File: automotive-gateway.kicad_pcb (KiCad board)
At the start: 2 copper layers, 101.6 x 88.9 mm, 103 parts, among them J3 Conn_01x02_Pin, Q1 AO3401A, Q2 2N7002, U1 STM32F405RGTx, U10 TJA1021xT, U11 TJA1021xT, U2 STM32F405RGTx, U3 ESP32-WROOM-32UE, U4 TJA1044GT-3, U5 TJA1044GT-3, U6 TJA1055T/3, U7 TJA1055T/3, U8 LM2596S-5, U9 AMS1117-3.3

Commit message: updated logo
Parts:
- moved G*** 1.26 mm to (107.8, 84.3)
- moved G*** 0.82 mm to (70.3, 20.4)
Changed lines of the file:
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@@
 	(footprint "Logos:logo_lhe"
 		(layer "F.Cu")
-		(at 108.0008 83.058 90)
+		(at 107.846144 84.310827 90)
 		(property "Reference" "G***"
 			(at 0 0 90)
@@
 	(footprint "mylib:logo_ag_12mm"
 		(layer "F.Cu")
-		(at 71.0692 20.2946)
+		(at 70.2564 20.4216)
 		(property "Reference" "G***"
 			(at 0 0 0)
@@
 			)
 		)
-		(property "Footprint" ""
+		(property "Datasheet" ""
 			(at 0 0 0)
-			(layer "F.SilkS")
+			(layer "F.Fab")
+			(hide yes)
+			(effects
+				(font
+					(size 1.27 1.27)
+				)
+			)
+		)
+		(property "Description" ""
+			(at 0 0 0)
+			(layer "F.Fab")
 			(hide yes)
 			(effects
 				(font
 					(size 1.27 1.27)
-					(thickness 0.15)
 				)
 			)
 		)
 		(attr board_only exclude_from_pos_files exclude_from_bom)
+		(duplicate_pad_numbers_are_jumpers no)
 		(fp_poly
 			(pts
-				(xy -5.3816 1.3626)
-				(xy -0.9847 1.3626)
-				(xy -0.4122 2.2787)
-				(xy -6.0000 2.2787)
+				(xy -5.3816 1.3626) (xy -0.9847 1.3626) (xy -0.4122 2.2787) (xy -6 2.2787)
 			)
 			(stroke
@@
 				(type default)
 			)
-			(fill solid)
+			(fill yes)
 			(layer "F.SilkS")
 		)
 		(fp_poly
 			(pts
-				(xy -5.1756 1.0878)
-				(xy -4.0535 1.0878)
-				(xy -3.6413 0.4924)
-				(xy -2.3816 0.4924)
-				(xy -2.3816 -0.4465)
-				(xy -3.0000 -0.4465)
-				(xy -2.3816 -1.3855)
-				(xy -2.3816 -2.2787)
-				(xy -2.9084 -2.2787)
+				(xy 0.5038 -1.019) (xy 1.7862 1.0878) (xy 0.687 1.0878) (xy -0.0458 -0.1488)
 			)
 			(stroke
@@
 				(type default)
 			)
-			(fill solid)
+			(fill yes)
 			(layer "F.SilkS")
 		)
 		(fp_poly
 			(pts
-				(xy -2.3816 -2.2787)
-				(xy -1.8091 -2.2787)
-				(xy 0.4580 1.3626)
-				(xy 2.4962 1.3626)
-				(xy 3.0229 0.5611)
-				(xy 2.0611 0.4924)
-				(xy 1.5114 -0.4237)
-				(xy 4.7862 -0.4237)
-				(xy 3.0229 2.2787)
-				(xy -0.0916 2.2787)
-				(xy -1.2138 0.4924)
-				(xy -2.3816 0.4924)
-				(xy -2.3816 -0.4465)
-				(xy -1.7862 -0.4465)
-				(xy -2.3816 -1.3855)
+				(xy -0.0916 -2.2787) (xy 6 -2.2787) (xy 5.4275 -1.3626) (xy 0.4122 -1.3626) (xy -0.2519 -0.3779)
+				(xy -0.8015 -1.2481)
 			)
 			(stroke
@@
 				(type default)
 			)
-			(fill solid)
+			(fill yes)
 			(layer "F.SilkS")
 		)
 		(fp_poly
 			(pts
-				(xy -0.0916 -2.2787)
-				(xy 6.0000 -2.2787)
-				(xy 5.4275 -1.3626)
-				(xy 0.4122 -1.3626)
-				(xy -0.2519 -0.3779)
-				(xy -0.8015 -1.2481)
+				(xy -5.1756 1.0878) (xy -4.0535 1.0878) (xy -3.6413 0.4924) (xy -2.3816 0.4924) (xy -2.3816 -0.4465)
+				(xy -3 -0.4465) (xy -2.3816 -1.3855) (xy -2.3816 -2.2787) (xy -2.9084 -2.2787)
 			)
 			(stroke
@@
 				(type default)
 			)
-			(fill solid)
+			(fill yes)
 			(layer "F.SilkS")
 		)
 		(fp_poly
 			(pts
-				(xy 0.5038 -1.0190)
-				(xy 1.7862 1.0878)
-				(xy 0.6870 1.0878)
-				(xy -0.0458 -0.1488)
+				(xy -2.3816 -2.2787) (xy -1.8091 -2.2787) (xy 0.458 1.3626) (xy 2.4962 1.3626) (xy 3.0229 0.5611)
+				(xy 2.0611 0.4924) (xy 1.5114 -0.4237) (xy 4.7862 -0.4237) (xy 3.0229 2.2787) (xy -0.0916 2.2787)
+				(xy -1.2138 0.4924) (xy -2.3816 0.4924) (xy -2.3816 -0.4465) (xy -1.7862 -0.4465) (xy -2.3816 -1.3855)
 			)
 			(stroke
@@
 				(type default)
 			)
-			(fill solid)
+			(fill yes)
 			(layer "F.SilkS")
 		)
+		(embedded_fonts no)
 	)
 	(footprint "Resistor_SMD:R_0805_2012Metric"

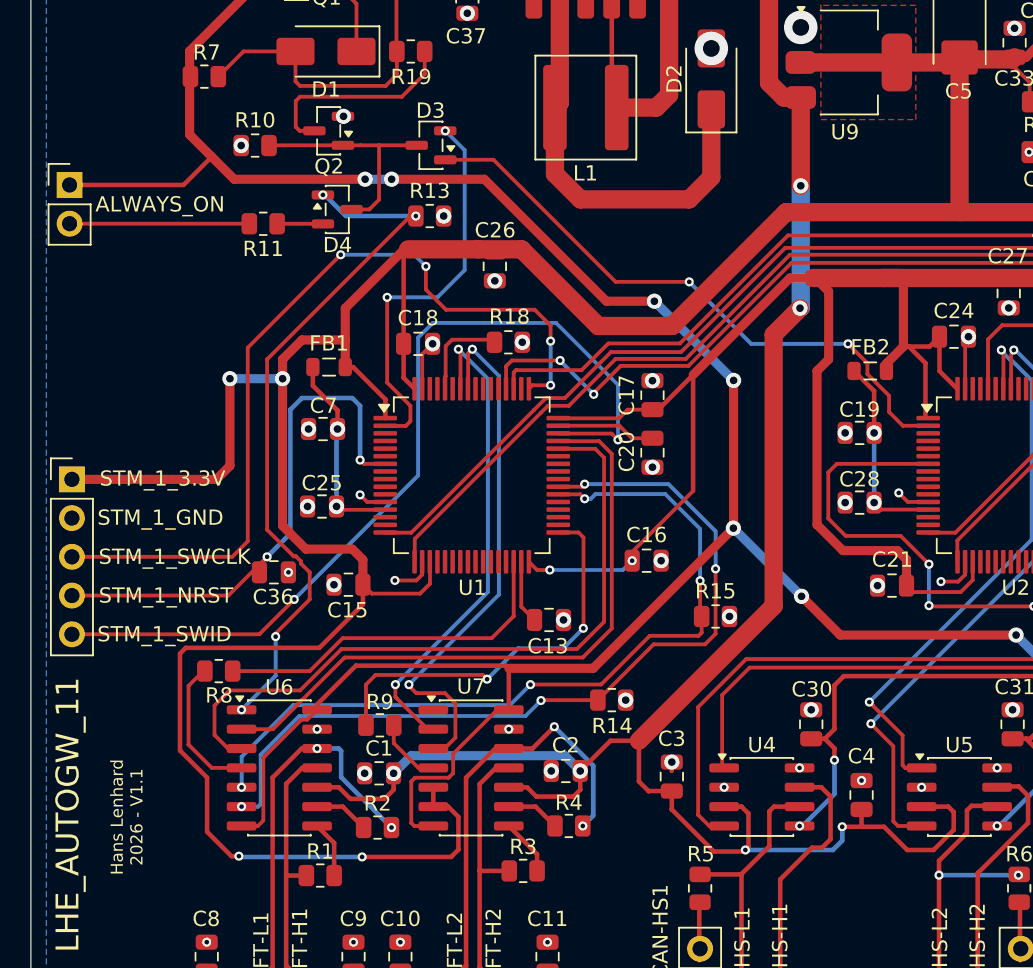
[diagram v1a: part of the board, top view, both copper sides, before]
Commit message: added external clock source
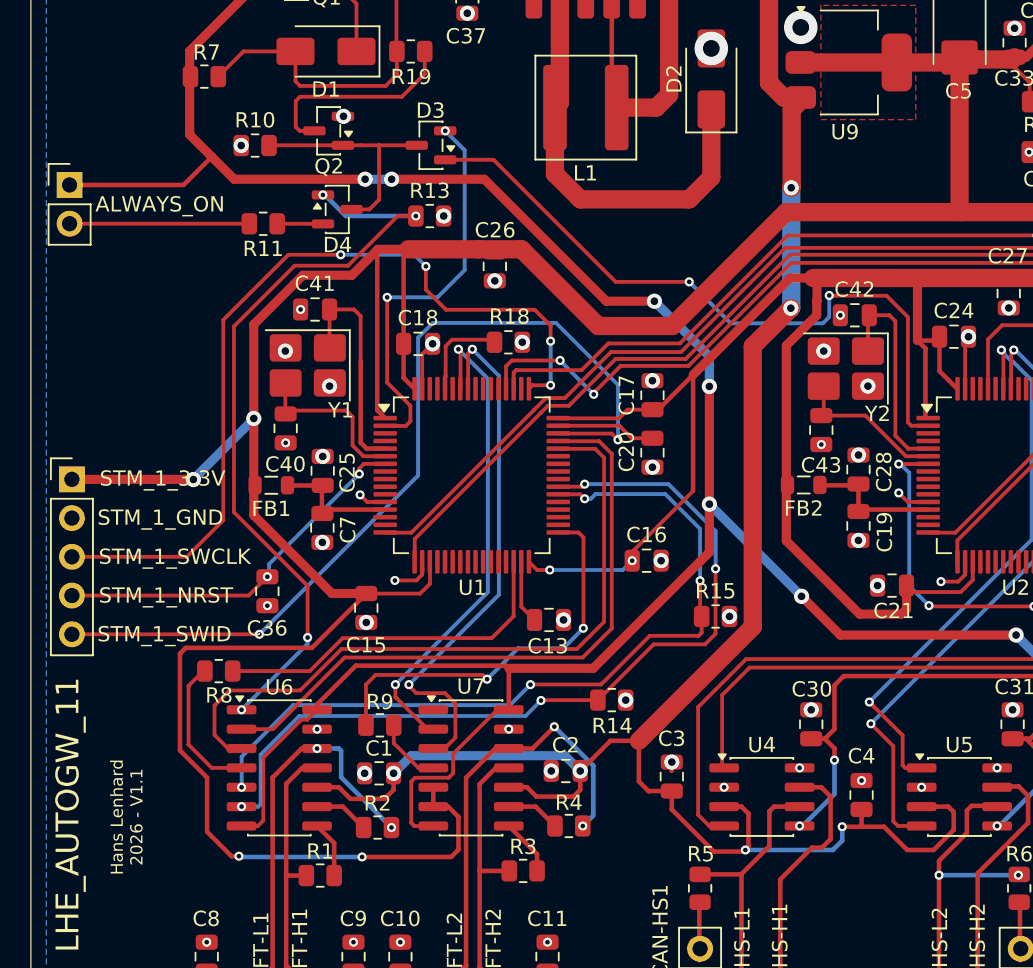
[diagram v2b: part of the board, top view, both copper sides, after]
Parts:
- added C40: 15pF, Capacitor_SMD:C_0805_2012Metric, F.Cu at (29.4, 57.9)
- added C41: 15pF, Capacitor_SMD:C_0805_2012Metric, F.Cu at (31.3, 50.1)
- added C42: 15pF, Capacitor_SMD:C_0805_2012Metric, F.Cu at (66.7, 50.5)
- added C43: 15pF, Capacitor_SMD:C_0805_2012Metric, F.Cu at (64.5, 58.0)
- added Y1: Crystal_GND24_Small, Crystal:Crystal_SMD_3225-4Pin_3.2x2.5mm_HandSoldering, F.Cu at (30.9, 53.7)
- added Y2: Crystal_GND24_Small, Crystal:Crystal_SMD_3225-4Pin_3.2x2.5mm_HandSoldering, F.Cu at (66.2, 54.0)
- moved FB2 8.66 mm to (63.4, 61.6), turned to 180 degrees
- moved FB1 8.63 mm to (28.5, 61.6), turned to 180 degrees
- moved C7 6.49 mm to (31.8, 64.4), turned to -90 degrees
- moved C19 6.10 mm to (67.0, 64.3), turned to -90 degrees
- moved C25 2.33 mm to (31.8, 60.7), turned to 90 degrees
- moved C28 2.17 mm to (67.0, 60.6), turned to 90 degrees
- moved C15 1.93 mm to (34.7, 69.7), turned to -90 degrees
- moved C36 1.31 mm to (28.2, 68.5), turned to -90 degrees
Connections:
- U1 pad 5: unconnected-(U1-PH0-Pad5) -> Net-(U1-PH0)
- U1 pad 6: unconnected-(U1-PH1-Pad6) -> Net-(U1-PH1)
- U2 pad 5: unconnected-(U2-PH0-Pad5) -> Net-(U2-PH0)
- U2 pad 6: unconnected-(U2-PH1-Pad6) -> Net-(U2-PH1)
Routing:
- net Net-(U1-PH0): track 0.00 -> 15.0 mm
- net Net-(U2-PH0): track 0.00 -> 14.3 mm
- net Net-(U1-PH1): track 0.00 -> 10.5 mm
- net Net-(U2-PH1): track 0.00 -> 10.3 mm
- net Net-(STM_FLASH1-Pin_4): track 34.7 -> 24.9 mm
- net Net-(STM_FLASH2-Pin_4): track 61.1 -> 52.9 mm
- net Net-(U2-PC13): track 39.9 -> 45.3 mm
- net Net-(U1-VDDA): track 13.1 -> 8.39 mm, vias 2 -> 0
- net Net-(U2-VDDA): track 12.9 -> 8.37 mm, vias 2 -> 0
- net Net-(U6-INH): track 46.4 -> 50.5 mm
- net /12V_Protected: track 234.3 -> 235.2 mm
- net /3.3V: track 496.9 -> 496.1 mm
- net /GND: track 17.0 -> 16.8 mm, vias 88 -> 96
